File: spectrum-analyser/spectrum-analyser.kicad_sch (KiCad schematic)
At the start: 23 parts, among them J1 Conn_Coaxial, Q1 PMOS, Q2 PMOS, Q5 Q_PMOS_GSD, SW2 SW_Push, SW3 SW_Push, SW4 SW_Push, SW5 SW_Push, SW6 SW_SPDT, U1 1.3" OLED, U2 LM1117MP-3.3, U3 ESP32-C3_Zero, U4 RX5808(V3.3)

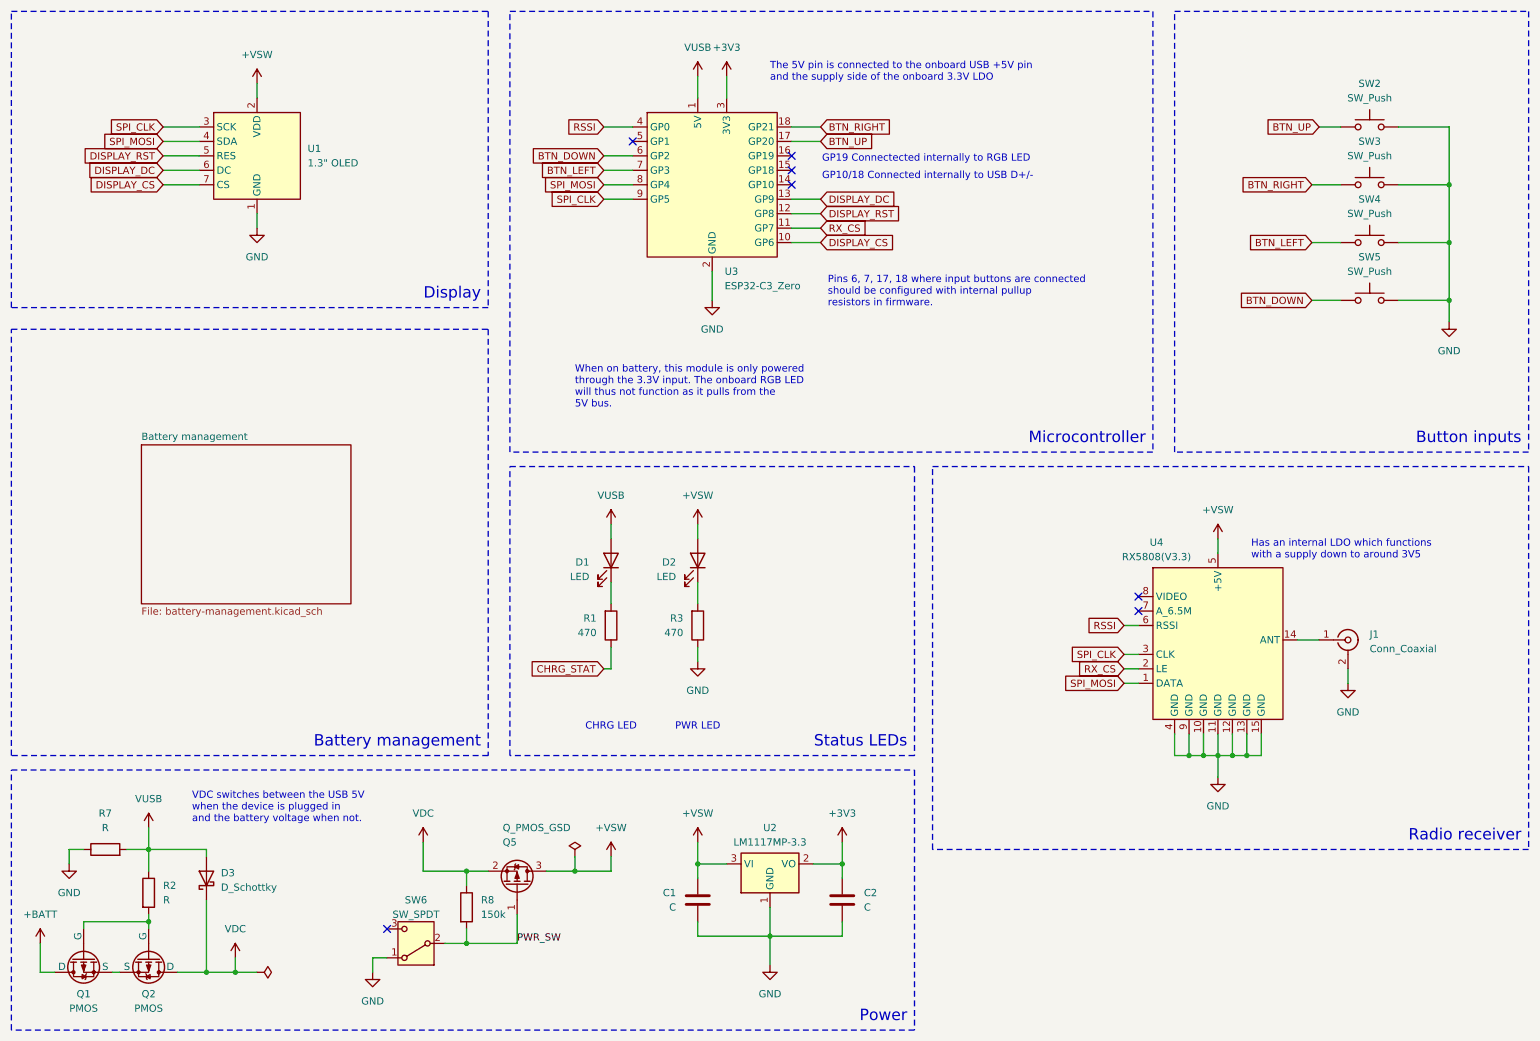
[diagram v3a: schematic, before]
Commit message: Assign component footprints
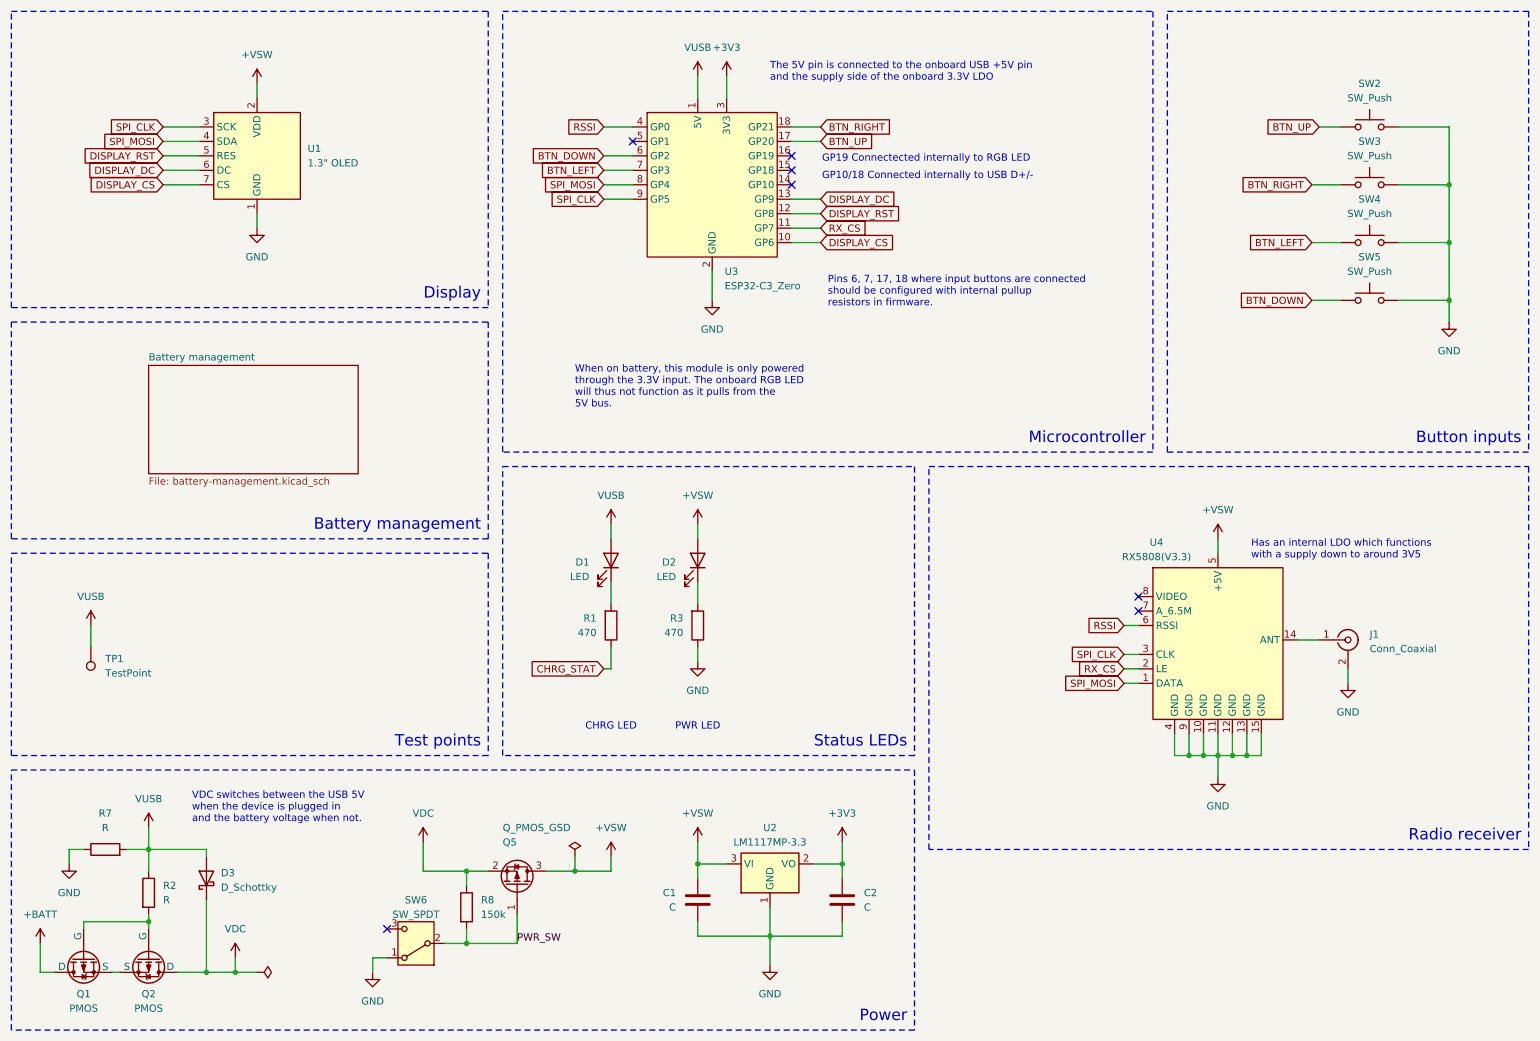
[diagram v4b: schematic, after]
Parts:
- added TP1: TestPoint, TestPoint:TestPoint_Pad_D3.0mm, symbol Connector:TestPoint
- C1, C2: footprint (none) -> Capacitor_SMD:C_0603_1608Metric_Pad1.08x0.95mm_HandSolder
- D1, D2: footprint (none) -> LED_SMD:LED_0603_1608Metric_Pad1.05x0.95mm_HandSolder
- D3: footprint (none) -> Diode_SMD:D_SMA_Handsoldering
- J1: footprint (none) -> Connector_Coaxial:SMA_Samtec_SMA-J-P-H-ST-EM1_EdgeMount
- Q1, Q2: footprint (none) -> Package_TO_SOT_SMD:SOT-23
- R1, R2, R3, R7: footprint (none) -> Resistor_SMD:R_0603_1608Metric_Pad0.98x0.95mm_HandSolder
- R8: footprint Resistor_SMD:R_0603_1608Metric -> Resistor_SMD:R_0603_1608Metric_Pad0.98x0.95mm_HandSolder
- SW2, SW3, SW4, SW5: footprint (none) -> Thanassis_Foot:SW_PUSH_ADAFRUIT_SMALL
- SW6: footprint thanassis_foot:SW_SPDT_TEC_1825232-1 -> Thanassis_Foot:SW_SPDT_TEC_1825232-1
- U1: footprint thanassis_foot:1.30 OLED -> Thanassis_Foot:1.30 OLED
- U3: footprint (none) -> Thanassis_Foot:ESP32-C3_Zero
- U4: footprint thanassis_foot:RX5808(V3.3) -> Thanassis_Foot:RX5808(V3.3)
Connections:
- net VUSB: now also TP1.1
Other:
- note added: "Test points"
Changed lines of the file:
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@@
 	(wire
 		(pts
+			(xy 29.21 123.19) (xy 29.21 127)
+		)
+		(stroke
+			(width 0)
+			(type default)
+		)
+	)
+	(wire
+		(pts
 			(xy 135.89 105.41) (xy 135.89 107.95)
 		)
@@
 	)
 	(rectangle
-		(start 102.87 15.24)
+		(start 101.6 15.24)
 		(end 215.9 92.71)
 		(stroke
@@
 	)
 	(rectangle
+		(start 15.24 110.49)
+		(end 99.06 146.05)
+		(stroke
+			(width 0)
+			(type dash)
+		)
+		(fill
+			(type none)
+		)
+	)
+	(rectangle
 		(start 15.24 15.24)
 		(end 99.06 67.31)
@@
 	)
 	(rectangle
-		(start 177.165 95.25)
+		(start 176.53 95.25)
 		(end 281.94 162.56)
 		(stroke
@@
 	)
 	(rectangle
-		(start 15.24 71.12)
-		(end 99.06 146.05)
+		(start 15.24 69.85)
+		(end 99.06 107.95)
 		(stroke
 			(width 0)
@@
 	)
 	(rectangle
-		(start 219.71 15.24)
+		(start 218.44 15.24)
 		(end 281.94 92.71)
 		(stroke
@@
 	)
 	(rectangle
-		(start 102.87 95.25)
+		(start 101.6 95.25)
 		(end 173.99 146.05)
 		(stroke
@@
 	(text "Battery management"
 		(exclude_from_sim no)
-		(at 97.79 144.78 0)
+		(at 97.79 106.68 0)
 		(effects
 			(font
@@
 		)
 	)
+	(text "Test points"
+		(exclude_from_sim no)
+		(at 97.79 144.78 0)
+		(effects
+			(font
+				(size 2 2)
+			)
+			(justify right bottom)
+		)
+	)
 	(text "Microcontroller"
 		(exclude_from_sim no)
@@
 			)
 		)
-		(property "Footprint" "Resistor_SMD:R_0603_1608Metric"
+		(property "Footprint" "Resistor_SMD:R_0603_1608Metric_Pad0.98x0.95mm_HandSolder"
 			(at 93.472 172.72 90)
 			(effects
@@
 			)
 		)
-		(property "Footprint" ""
+		(property "Footprint" "Thanassis_Foot:SW_PUSH_ADAFRUIT_SMALL"
 			(at 254 50.8 0)
 			(effects
@@
 			)
 		)
-		(property "Footprint" ""
+		(property "Footprint" "Connector_Coaxial:SMA_Samtec_SMA-J-P-H-ST-EM1_EdgeMount"
 			(at 250.19 125.73 0)
 			(effects
@@
 			)
 		)
-		(property "Footprint" ""
+		(property "Footprint" "Thanassis_Foot:SW_PUSH_ADAFRUIT_SMALL"
 			(at 254 40.64 0)
 			(effects
@@
 			)
 		)
-		(property "Footprint" ""
+		(property "Footprint" "Package_TO_SOT_SMD:SOT-23"
 			(at 25.4 186.69 0)
 			(effects
@@
 			)
 		)
-		(property "Footprint" ""
+		(property "Footprint" "Diode_SMD:D_SMA_Handsoldering"
 			(at 49.53 167.64 0)
 			(effects
@@
 			)
 		)
-		(property "Footprint" ""
+		(property "Footprint" "Package_TO_SOT_SMD:SOT-23"
 			(at 41.91 186.69 0)
 			(effects
@@
 			)
 		)
-		(property "Footprint" ""
+		(property "Footprint" "Capacitor_SMD:C_0603_1608Metric_Pad1.08x0.95mm_HandSolder"
 			(at 162.2552 175.26 0)
 			(effects
@@
 			)
 		)
-		(property "Footprint" ""
+		(property "Footprint" "Capacitor_SMD:C_0603_1608Metric_Pad1.08x0.95mm_HandSolder"
 			(at 134.9248 175.26 0)
 			(effects
@@
 			)
 		)
-		(property "Footprint" ""
+		(property "Footprint" "LED_SMD:LED_0603_1608Metric_Pad1.05x0.95mm_HandSolder"
 			(at 120.65 111.76 0)
 			(effects
@@
 			)
 		)
-		(property "Footprint" ""
+		(property "Footprint" "Resistor_SMD:R_0603_1608Metric_Pad0.98x0.95mm_HandSolder"
 			(at 37.592 170.18 90)
 			(effects
@@
 			)
 		)
-		(property "Footprint" ""
+		(property "Footprint" "Resistor_SMD:R_0603_1608Metric_Pad0.98x0.95mm_HandSolder"
 			(at 134.112 123.19 90)
 			(effects
@@
 	)
 	(symbol
+		(lib_id "Connector:TestPoint")
+		(at 29.21 127 180)
+		(unit 1)
+		(exclude_from_sim no)
+		(in_bom yes)
+		(on_board yes)
+		(dnp no)
+		(fields_autoplaced yes)
+		(property "Reference" "TP1"
+			(at 31.75 129.0319 0)
+			(effects
+				(font
+					(size 1.27 1.27)
+				)
+				(justify right)
+			)
+		)
+		(property "Value" "TestPoint"
+			(at 31.75 131.5719 0)
+			(effects
+				(font
+					(size 1.27 1.27)
+				)
+				(justify right)
+			)
+		)
+		(property "Footprint" "TestPoint:TestPoint_Pad_D3.0mm"
+			(at 24.13 127 0)
+			(effects
+				(font
+					(size 1.27 1.27)
+				)
+				(hide yes)
+			)
+		)
+		(property "Datasheet" "~"
+			(at 24.13 127 0)
+			(effects
+				(font
+					(size 1.27 1.27)
+				)
+				(hide yes)
+			)
+		)
+		(property "Description" "test point"
+			(at 29.21 127 0)
+			(effects
+				(font
+					(size 1.27 1.27)
+				)
+				(hide yes)
+			)
+		)
+		(pin "1"
+		)
+		(instances
+			(project ""
+				(path "/e63e39d7-6ac0-4ffd-8aa3-1841a4541b55"
+					(reference "TP1")
+					(unit 1)
+				)
+			)
+		)
+	)
+	(symbol
 		(lib_id "Device:LED")
 		(at 135.89 111.76 270)
@@
 			)
 		)
-		(property "Footprint" ""
+		(property "Footprint" "LED_SMD:LED_0603_1608Metric_Pad1.05x0.95mm_HandSolder"
 			(at 135.89 111.76 0)
 			(effects
@@
 			)
 		)
-		(property "Footprint" ""
+		(property "Footprint" "Resistor_SMD:R_0603_1608Metric_Pad0.98x0.95mm_HandSolder"
 			(at 31.75 164.338 90)
 			(effects
@@
 			)
 		)
-		(property "Footprint" ""
+		(property "Footprint" "Thanassis_Foot:SW_PUSH_ADAFRUIT_SMALL"
 			(at 254 30.48 0)
 			(effects
@@
 			)
 		)
-		(property "Footprint" "thanassis_foot:1.30 OLED"
+		(property "Footprint" "Thanassis_Foot:1.30 OLED"
 			(at 55.88 36.83 0)
 			(effects
@@
 			)
 		)
-		(property "Footprint" ""
+		(property "Footprint" "Thanassis_Foot:ESP32-C3_Zero"
 			(at 138.43 45.72 0)
 			(effects
@@
 	)
 	(symbol
+		(lib_id "thanassis_sym:VUSB")
+		(at 29.21 123.19 0)
+		(unit 1)
+		(exclude_from_sim no)
+		(in_bom yes)
+		(on_board yes)
+		(dnp no)
+		(fields_autoplaced yes)
+		(property "Reference" "#PWR016"
+			(at 29.21 127 0)
+			(effects
+				(font
+					(size 1.27 1.27)
+				)
+				(hide yes)
+			)
+		)
+		(property "Value" "VUSB"
+			(at 29.21 118.11 0)
+			(effects
+				(font
+					(size 1.27 1.27)
+				)
+			)
+		)
+		(property "Footprint" ""
+			(at 29.21 123.19 0)
+			(effects
+				(font
+					(size 1.27 1.27)
+				)
+				(hide yes)
+			)
+		)
+		(property "Datasheet" ""
+			(at 29.21 123.19 0)
+			(effects
+				(font
+					(size 1.27 1.27)
+				)
+				(hide yes)
+			)
+		)
+		(property "Description" "Power symbol creates a global label with name \"VUSB\""
+			(at 29.21 123.19 0)
+			(effects
+				(font
+					(size 1.27 1.27)
+				)
+				(hide yes)
+			)
+		)
+		(pin "1"
+		)
+		(instances
+			(project "spectrum-analyser"
+				(path "/e63e39d7-6ac0-4ffd-8aa3-1841a4541b55"
+					(reference "#PWR016")
+					(unit 1)
+				)
+			)
+		)
+	)
+	(symbol
 		(lib_id "power:GND")
 		(at 267.97 69.85 0)
@@
 			)
 		)
-		(property "Footprint" "thanassis_foot:RX5808(V3.3)"
+		(property "Footprint" "Thanassis_Foot:RX5808(V3.3)"
 			(at 245.11 110.49 0)
 			(effects
@@
 			)
 		)
-		(property "Footprint" ""
+		(property "Footprint" "Thanassis_Foot:SW_PUSH_ADAFRUIT_SMALL"
 			(at 254 60.96 0)
 			(effects
@@
 			)
 		)
-		(property "Footprint" "thanassis_foot:SW_SPDT_TEC_1825232-1"
+		(property "Footprint" "Thanassis_Foot:SW_SPDT_TEC_1825232-1"
 			(at 86.36 179.07 0)
 			(effects
@@
 			)
 		)
-		(property "Footprint" ""
+		(property "Footprint" "Resistor_SMD:R_0603_1608Metric_Pad0.98x0.95mm_HandSolder"
 			(at 118.872 123.19 90)
 			(effects
@@
 	)
 	(sheet
-		(at 38.1 91.44)
-		(size 36.83 27.94)
+		(at 39.37 77.47)
+		(size 36.83 19.05)
 		(fields_autoplaced yes)
 		(stroke
@@
 		)
 		(property "Sheetname" "Battery management"
-			(at 38.1 90.7284 0)
+			(at 39.37 76.7584 0)
 			(effects
 				(font
@@
 		)
 		(property "Sheetfile" "battery-management.kicad_sch"
-			(at 38.1 119.9646 0)
+			(at 39.37 97.1046 0)
 			(effects
 				(font

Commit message: Start initial PCB layout
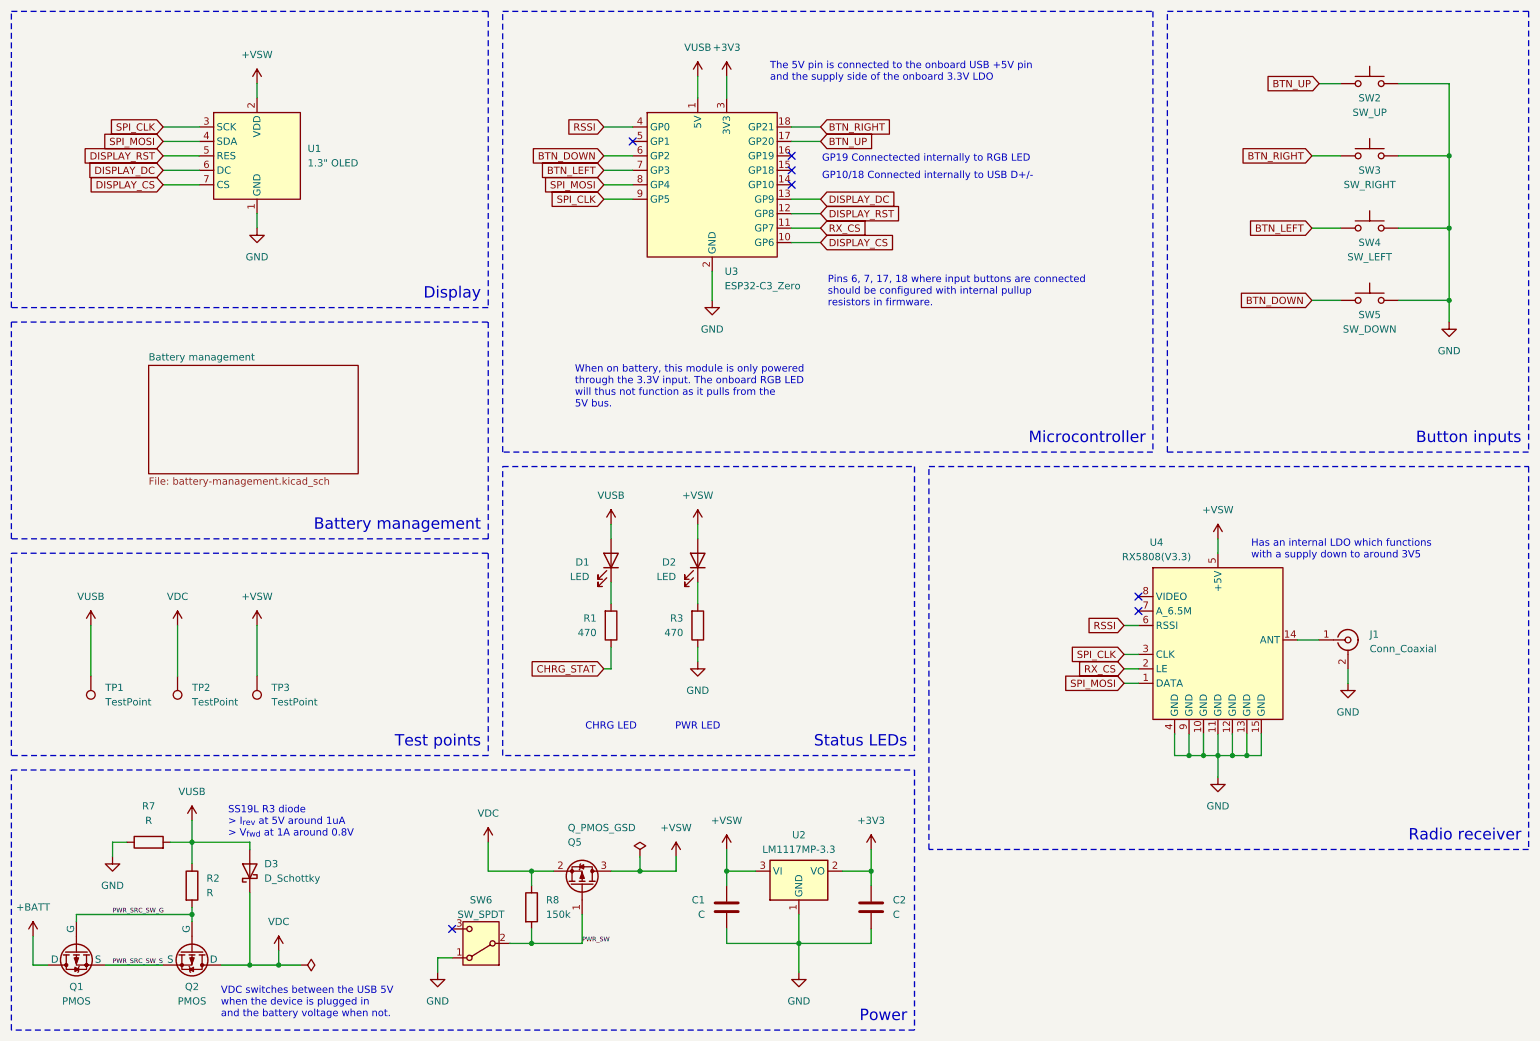
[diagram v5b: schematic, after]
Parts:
- added TP2, TP3: TestPoint, TestPoint:TestPoint_Pad_D3.0mm, symbol Connector:TestPoint
- SW2: value SW_Push -> SW_UP
- SW3: value SW_Push -> SW_RIGHT
- SW4: value SW_Push -> SW_LEFT
- SW5: value SW_Push -> SW_DOWN
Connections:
- net +VSW: now also TP3.1
- net VDC: now also TP2.1
- net PWR_SRC_SW_G: now reaches Q1.2 (G), Q2.2 (G), R2.2
- net PWR_SRC_SW_S: now reaches Q1.3 (S), Q2.3 (S)
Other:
- note added: "SS19L R3 diode > I_{rev} at 5V around 1uA > V_{fwd} at 1A around 0.8V"
- moved on the sheet: C1, C2, D3, Q1, Q2, Q5, R2, R7, R8, SW2, SW3, SW4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

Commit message: Improve PCB layout
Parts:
- renumbered D3 to D1, D1 to D2, D2 to D3, Q5 to Q3, R7 to R1, R8 to R3, R1 to R4, R3 to R5, SW6 to SW1, U3 to U2, U2 to U3
